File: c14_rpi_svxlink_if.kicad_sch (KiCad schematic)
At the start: 52 parts, among them J1 RPi_GPIO Tall, J2 Conn_01x04, J3 Conn_01x04, J4 Conn_01x04, J5 Conn_01x02, J6 Conn_01x04, J7 DB9F, Q1 BC847, Q2 BC847, Q3 BC847, Q4 BC857, T1 1:1, T2 1:1, U1 TLP222A o. AQY282EH, U2 HCPL-B17, U3 ADS1115_Module

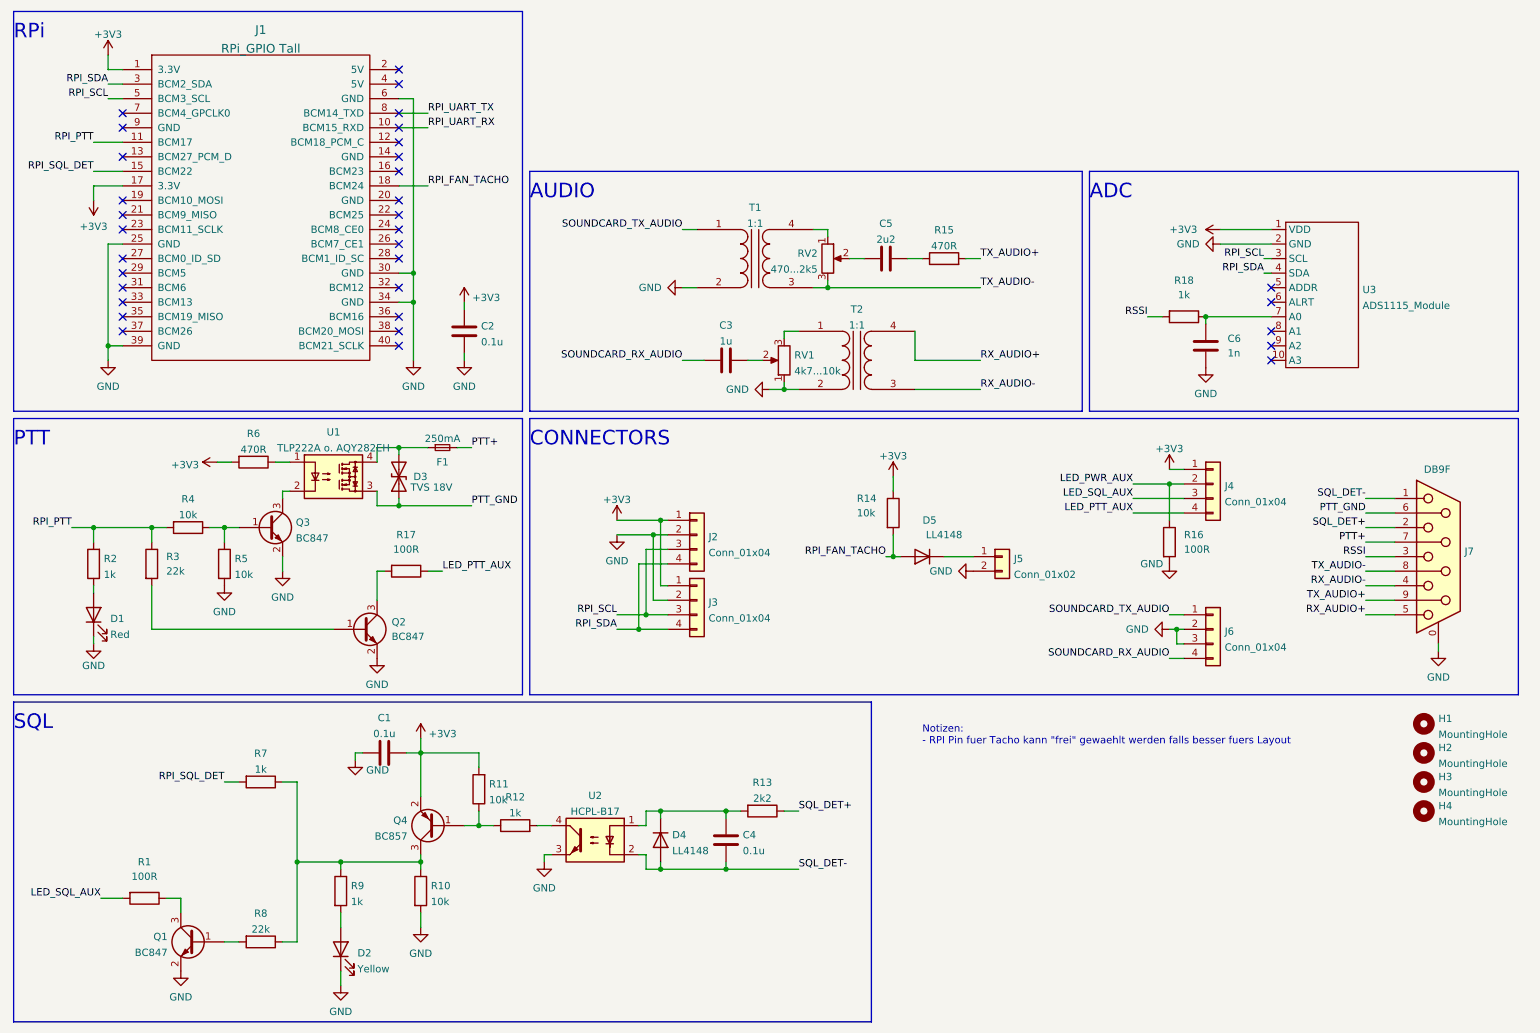
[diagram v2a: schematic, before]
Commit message: Add Open Collector for Fan Ctrl
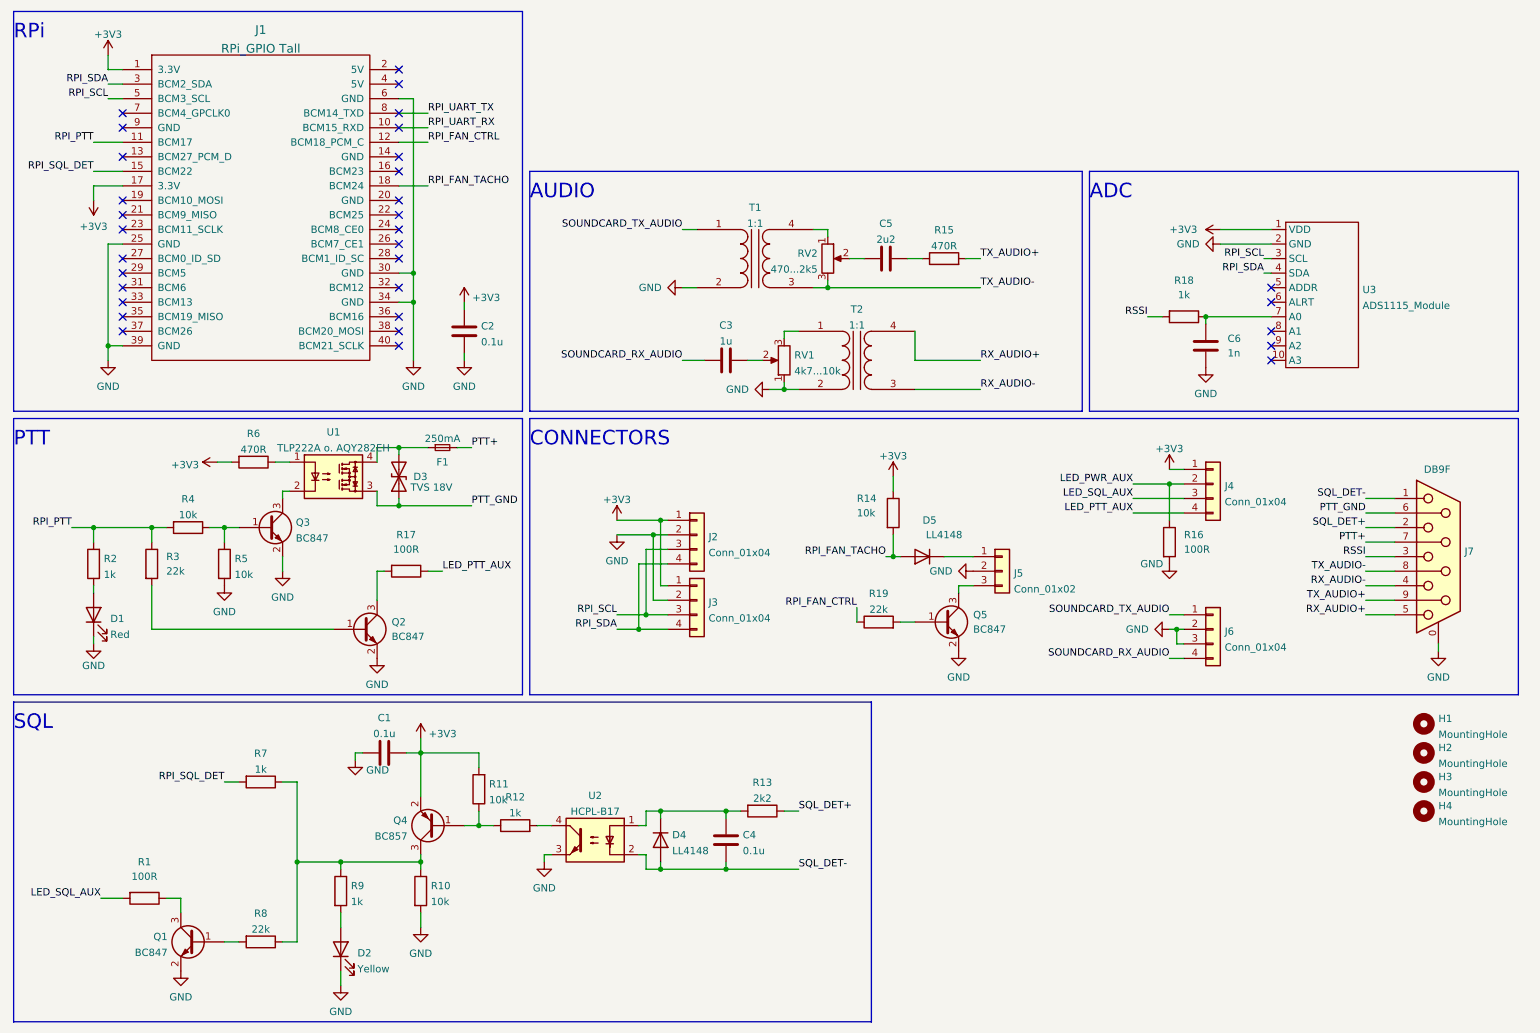
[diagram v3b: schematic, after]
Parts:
- added Q5: BC847, Package_TO_SOT_SMD:SOT-23, symbol Transistor_BJT:BC847
- added R19: 22k, Resistor_SMD:R_0805_2012Metric_Pad1.20x1.40mm_HandSolder, symbol Device:R
- J5: footprint Connector_JST:JST_XH_B2B-XH-A_1x02_P2.50mm_Vertical -> Connector_JST:JST_XH_B3B-XH-A_1x03_P2.50mm_Vertical; symbol Connector_Generic:Conn_01x02 -> Connector_Generic:Conn_01x03
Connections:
- net GND: now also Q5.2 (E)
- net RPI_FAN_CTRL: now reaches J1.12 (BCM18_PCM_C)
- net RPI_FAN_CTRL: now also R19.1
- new net: Q5.1 (B), R19.2
- new net: J5.3 (Pin_3), Q5.3 (C)
- no-connect marks 33 -> 32
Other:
- note removed: "Notizen: - RPI Pin fuer Tacho kann "frei" gewaehlt werden falls besser fuers Layout"
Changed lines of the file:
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@@
   (no_connect (at 86.36 77.47))
   (no_connect (at 86.36 54.61))
-  (no_connect (at 86.36 41.91))
-  (no_connect (at 86.36 46.99))
   (no_connect (at 86.36 52.07))
   (no_connect (at 238.76 67.31))
   (no_connect (at 86.36 31.75))
   (no_connect (at 86.36 29.21))
+  (no_connect (at 86.36 46.99))
   (no_connect (at 238.76 80.01))
   (no_connect (at 238.76 74.93))
@@
     (stroke (width 0) (type default) (color 0 0 0 0))
   )
+  (wire (pts (xy 184.15 119.38) (xy 184.15 120.65))
+    (stroke (width 0) (type default) (color 0 0 0 0))
+  )
   (wire (pts (xy 76.2 176.53) (xy 76.2 179.07))
     (stroke (width 0) (type default) (color 0 0 0 0))
@@
     (stroke (width 0) (type default) (color 0 0 0 0))
   )
+  (wire (pts (xy 86.36 41.91) (xy 91.44 41.91))
+    (stroke (width 0) (type default) (color 0 0 0 0))
+  )
   (wire (pts (xy 172.72 114.3) (xy 173.99 114.3))
     (stroke (width 0) (type default) (color 0 0 0 0))
@@
     (stroke (width 0) (type default) (color 0 0 0 0))
   )
+  (wire (pts (xy 173.99 125.73) (xy 176.53 125.73))
+    (stroke (width 0) (type default) (color 0 0 0 0))
+  )
   (wire (pts (xy 267.97 129.54) (xy 267.97 130.81))
     (stroke (width 0) (type default) (color 0 0 0 0))
   )
+  (wire (pts (xy 166.37 123.19) (xy 166.37 125.73))
+    (stroke (width 0) (type default) (color 0 0 0 0))
+  )
   (wire (pts (xy 181.61 114.3) (xy 186.69 114.3))
     (stroke (width 0) (type default) (color 0 0 0 0))
@@
   )
   (wire (pts (xy 43.18 127) (xy 74.93 127))
+    (stroke (width 0) (type default) (color 0 0 0 0))
+  )
+  (wire (pts (xy 186.69 119.38) (xy 184.15 119.38))
     (stroke (width 0) (type default) (color 0 0 0 0))
   )
@@
     (effects (font (size 2.54 2.54)) (justify left bottom))
   )
-  (text "Notizen:\n- RPI Pin fuer Tacho kann \"frei\" gewaehlt werden falls besser fuers Layout"
-    (at 177.8 147.32 0)
-    (effects (font (size 1.27 1.27)) (justify left bottom))
-  )
   (text "PTT" (at 19.05 95.25 0)
     (effects (font (size 2.54 2.54)) (justify left bottom))
@@
     (effects (font (size 1.27 1.27)) (justify left bottom))
   )
+  (label "RPI_FAN_CTRL" (at 91.44 41.91 0)
+    (effects (font (size 1.27 1.27)) (justify left bottom))
+  )
   (label "LED_SQL_AUX" (at 34.29 173.99 180)
     (effects (font (size 1.27 1.27)) (justify right bottom))
@@
   (label "SQL_DET-" (at 156.21 168.91 0)
     (effects (font (size 1.27 1.27)) (justify left bottom))
+  )
+  (label "RPI_FAN_CTRL" (at 166.37 123.19 180)
+    (effects (font (size 1.27 1.27)) (justify right bottom))
   )
   (label "PTT+" (at 255.27 111.76 180)
@@
     )
   )
+  (symbol (lib_id "Device:R") (at 170.18 125.73 90) (unit 1)
+    (in_bom yes) (on_board yes) (fields_autoplaced)
+    (property "Reference" "R19" (id 0) (at 170.18 120.7475 90))
+    (property "Value" "22k" (id 1) (at 170.18 123.5226 90))
+    (property "Footprint" "Resistor_SMD:R_0805_2012Metric_Pad1.20x1.40mm_HandSolder" (id 2) (at 170.18 127.508 90)
+      (effects (font (size 1.27 1.27)) hide)
+    )
+    (property "Datasheet" "~" (id 3) (at 170.18 125.73 0)
+      (effects (font (size 1.27 1.27)) hide)
+    )
+    (property "PartNr_Mouser" "603-RC0805FR-0722KL" (id 4) (at 170.18 125.73 0)
+      (effects (font (size 1.27 1.27)) hide)
+    )
+    (pin "1")
+    (pin "2")
+  )
   (symbol (lib_id "power:+3V3") (at 97.79 69.85 0) (unit 1)
     (in_bom yes) (on_board yes) (fields_autoplaced)
@@
     (pin "1")
   )
-  (symbol (lib_id "Connector_Generic:Conn_01x02") (at 191.77 114.3 0) (unit 1)
-    (in_bom yes) (on_board yes) (fields_autoplaced)
-    (property "Reference" "J5" (id 0) (at 193.802 114.6615 0)
-      (effects (font (size 1.27 1.27)) (justify left))
-    )
-    (property "Value" "Conn_01x02" (id 1) (at 193.802 117.4366 0)
-      (effects (font (size 1.27 1.27)) (justify left))
-    )
-    (property "Footprint" "Connector_JST:JST_XH_B2B-XH-A_1x02_P2.50mm_Vertical" (id 2) (at 191.77 114.3 0)
-      (effects (font (size 1.27 1.27)) hide)
-    )
-    (property "Datasheet" "~" (id 3) (at 191.77 114.3 0)
-      (effects (font (size 1.27 1.27)) hide)
-    )
-    (pin "1")
-    (pin "2")
+  (symbol (lib_id "Connector_Generic:Conn_01x03") (at 191.77 116.84 0) (unit 1)
+    (in_bom yes) (on_board yes) (fields_autoplaced)
+    (property "Reference" "J5" (id 0) (at 193.802 117.2015 0)
+      (effects (font (size 1.27 1.27)) (justify left))
+    )
+    (property "Value" "Conn_01x02" (id 1) (at 193.802 119.9766 0)
+      (effects (font (size 1.27 1.27)) (justify left))
+    )
+    (property "Footprint" "Connector_JST:JST_XH_B3B-XH-A_1x03_P2.50mm_Vertical" (id 2) (at 191.77 116.84 0)
+      (effects (font (size 1.27 1.27)) hide)
+    )
+    (property "Datasheet" "~" (id 3) (at 191.77 116.84 0)
+      (effects (font (size 1.27 1.27)) hide)
+    )
+    (pin "1")
+    (pin "2")
+    (pin "3")
   )
   (symbol (lib_id "Device:C") (at 143.51 80.01 270) (unit 1)
@@
     (pin "1")
   )
+  (symbol (lib_id "Transistor_BJT:BC847") (at 181.61 125.73 0) (unit 1)
+    (in_bom yes) (on_board yes) (fields_autoplaced)
+    (property "Reference" "Q5" (id 0) (at 186.69 124.4599 0)
+      (effects (font (size 1.27 1.27)) (justify left))
+    )
+    (property "Value" "BC847" (id 1) (at 186.69 126.9999 0)
+      (effects (font (size 1.27 1.27)) (justify left))
+    )
+    (property "Footprint" "Package_TO_SOT_SMD:SOT-23" (id 2) (at 186.69 127.635 0)
+      (effects (font (size 1.27 1.27) italic) (justify left) hide)
+    )
+    (property "Datasheet" "http://www.infineon.com/dgdl/Infineon-BC847SERIES_BC848SERIES_BC849SERIES_BC850SERIES-DS-v01_01-en.pdf?fileId=db3a304314dca389011541d4630a1657" (id 3) (at 181.61 125.73 0)
+      (effects (font (size 1.27 1.27)) (justify left) hide)
+    )
+    (property "PartNr_Mouser" "771-BC847235" (id 4) (at 181.61 125.73 0)
+      (effects (font (size 1.27 1.27)) hide)
+    )
+    (pin "1")
+    (pin "2")
+    (pin "3")
+  )
   (symbol (lib_id "Device:R") (at 60.96 97.79 270) (unit 1)
     (in_bom yes) (on_board yes) (fields_autoplaced)
@@
     (pin "2")
   )
+  (symbol (lib_id "power:GND") (at 184.15 130.81 0) (unit 1)
+    (in_bom yes) (on_board yes) (fields_autoplaced)
+    (property "Reference" "#PWR031" (id 0) (at 184.15 137.16 0)
+      (effects (font (size 1.27 1.27)) hide)
+    )
+    (property "Value" "GND" (id 1) (at 184.15 135.3725 0))
+    (property "Footprint" "" (id 2) (at 184.15 130.81 0)
+      (effects (font (size 1.27 1.27)) hide)
+    )
+    (property "Datasheet" "" (id 3) (at 184.15 130.81 0)
+      (effects (font (size 1.27 1.27)) hide)
+    )
+    (pin "1")
+  )
   (symbol (lib_id "power:GND") (at 78.74 149.86 0) (unit 1)
     (in_bom yes) (on_board yes) (fields_autoplaced)
@@
       (reference "#PWR030") (unit 1) (value "+3V3") (footprint "")
     )
+    (path "/d8fbedd9-bbf3-4187-842a-3510bcba1e5f"
+      (reference "#PWR031") (unit 1) (value "GND") (footprint "")
+    )
     (path "/d7715fde-6f0b-46cf-9dde-1798ae531e5a"
       (reference "C1") (unit 1) (value "0.1u") (footprint "Capacitor_SMD:C_0805_2012Metric_Pad1.18x1.45mm_HandSolder")
@@
     )
     (path "/58956415-360b-40f7-803b-b6f3cb064aa6"
-      (reference "J5") (unit 1) (value "Conn_01x02") (footprint "Connector_JST:JST_XH_B2B-XH-A_1x02_P2.50mm_Vertical")
+      (reference "J5") (unit 1) (value "Conn_01x02") (footprint "Connector_JST:JST_XH_B3B-XH-A_1x03_P2.50mm_Vertical")
     )
     (path "/529e174a-9525-49fa-9570-9a824abc0712"
@@
       (reference "Q4") (unit 1) (value "BC857") (footprint "Package_TO_SOT_SMD:SOT-23")
     )
+    (path "/98c41d91-3f72-4f82-8376-ce2f310a6d96"
+      (reference "Q5") (unit 1) (value "BC847") (footprint "Package_TO_SOT_SMD:SOT-23")
+    )
     (path "/9fee11bc-5830-4e56-b0e4-2a78e387f58b"
       (reference "R1") (unit 1) (value "100R") (footprint "Resistor_SMD:R_0805_2012Metric_Pad1.20x1.40mm_HandSolder")
@@
       (reference "R18") (unit 1) (value "1k") (footprint "Resistor_SMD:R_0805_2012Metric_Pad1.20x1.40mm_HandSolder")
     )
+    (path "/3fdc1205-170d-4bad-a583-c2274b810ac0"
+      (reference "R19") (unit 1) (value "22k") (footprint "Resistor_SMD:R_0805_2012Metric_Pad1.20x1.40mm_HandSolder")
+    )
     (path "/54545e51-e802-4511-9bf4-469b9f2f2d3a"

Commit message: Neue Teile platziert, pre-1.1 bereit fuer Review
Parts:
- removed Q5: BC847, Package_TO_SOT_SMD:SOT-23, symbol Transistor_BJT:BC847
- added C7, C8: 1n, Capacitor_SMD:C_0805_2012Metric_Pad1.18x1.45mm_HandSolder, symbol Device:C
- added D6, D7: LL4148, Diode_SMD:D_MiniMELF, symbol Diode:LL4148
- added FID1, FID2, FID3: Fiducial, Fiducial:Fiducial_1mm_Mask3mm, symbol Mechanical:Fiducial
- added J8: Conn_01x01_Male, Connector_PinHeader_2.54mm:PinHeader_1x01_P2.54mm_Vertical, symbol Connector:Conn_01x01_Male
- added JP1, JP2: SolderJumper_2_Open, Jumper:SolderJumper-2_P1.3mm_Open_TrianglePad1.0x1.5mm, symbol Jumper:SolderJumper_2_Open
- added LOGO1: Logo_Open_Hardware_Small, Symbol:OSHW-Logo2_9.8x8mm_SilkScreen, symbol Graphic:Logo_Open_Hardware_Small
- added Q5: IRLML0030, Package_TO_SOT_SMD:SOT-23, symbol Transistor_FET:IRLML0030
- added R20: 10k, Resistor_SMD:R_0805_2012Metric_Pad1.20x1.40mm_HandSolder, symbol Device:R
- added TP1: Conn_01x09_Male, Connector_PinHeader_1.27mm:PinHeader_1x09_P1.27mm_Vertical, symbol Connector:Conn_01x09_Male
- added TP2: Conn_01x03_Male, Connector_PinHeader_1.27mm:PinHeader_1x03_P1.27mm_Vertical, symbol Connector:Conn_01x03_Male
- R19: value 22k -> 1k
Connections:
- net GND: now also J8.1 (Pin_1), JP1.1 (A), Q5.2 (S), R20.2, TP2.2 (Pin_2)
- net PTT+: now also TP1.4 (Pin_4)
- net PTT_GND: now also TP1.2 (Pin_2)
- net RPI_FAN_CTRL: now also R20.1
- net RSSI: now also TP1.5 (Pin_5)
- net RX_AUDIO+: now also C8.2, JP2.2 (B), TP1.9 (Pin_9)
- net RX_AUDIO-: now also C8.1, D6.1 (K), D7.2 (A), TP1.7 (Pin_7)
- net SOUNDCARD_RX_AUDIO: now also TP2.3 (Pin_3)
- net SOUNDCARD_TX_AUDIO: now also TP2.1 (Pin_1)
- net SQL_DET+: now also TP1.3 (Pin_3)
- net SQL_DET-: now also TP1.1 (Pin_1)
- net TX_AUDIO+: now also C7.2, TP1.8 (Pin_8)
- net TX_AUDIO-: now also C7.1, TP1.6 (Pin_6)
- net at R19.2: now also Q5.1 (G)
- net at J5.1 (Pin_1): now also JP1.2 (B), Q5.3 (D); no longer D5.1 (K)
- net at J5.3 (Pin_3): now also D5.1 (K)
- new net: D6.2 (A), D7.1 (K), JP2.1 (A)
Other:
- moved on the sheet: C3, D5, J5, J6, J7, R14, R15, R19, RV1, T2

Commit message: ready for production
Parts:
- added C9: 1n, Capacitor_SMD:C_0805_2012Metric_Pad1.18x1.45mm_HandSolder, symbol Device:C
- added R21: 100R, Resistor_SMD:R_0805_2012Metric_Pad1.20x1.40mm_HandSolder, symbol Device:R
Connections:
- net GND: now also C9.1
- net at Q5.1 (G), R19.2: now also C9.2
- net at D6.2 (A), D7.1 (K): now also R21.2; no longer JP2.1 (A)
- new net: JP2.1 (A), R21.1
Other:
- moved on the sheet: J2, J3, R19, R20

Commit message: last changes for 1.1
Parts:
- Q5: PartNr_Mouser (none) -> 942-IRLML0030TRPBF
- R19: PartNr_Mouser 603-RC0805FR-0722KL -> 652-CR0805FX-1001ELF
- R20: PartNr_Mouser (none) -> 603-RC0805JR-0710KL
- R21: PartNr_Mouser 652-CR0805FX-4700ELF -> 603-RC0805JR-07100RL
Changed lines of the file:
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@@
+      (effects (font (size 1.27 1.27)) hide)
+    )
+    (property "PartNr_Mouser" "603-RC0805JR-0710KL" (id 4) (at 156.21 129.54 0)
       (effects (font (size 1.27 1.27)) hide)
     )
@@
       (effects (font (size 1.27 1.27)) hide)
     )
-    (property "PartNr_Mouser" "603-RC0805FR-0722KL" (id 4) (at 161.29 124.46 0)
+    (property "PartNr_Mouser" "652-CR0805FX-1001ELF" (id 4) (at 161.29 124.46 0)
       (effects (font (size 1.27 1.27)) hide)
     )
@@
       (effects (font (size 1.27 1.27)) (justify left) hide)
     )
+    (property "PartNr_Mouser" "942-IRLML0030TRPBF" (id 4) (at 181.61 124.46 0)
+      (effects (font (size 1.27 1.27)) hide)
+    )
     (pin "1")
     (pin "2")
@@
       (effects (font (size 1.27 1.27)) hide)
     )
-    (property "PartNr_Mouser" "652-CR0805FX-4700ELF" (id 4) (at 170.18 77.47 0)
-      (effects (font (size 1.27 1.27)) hide)
-    )
+    (property "PartNr_Mouser" "603-RC0805JR-07100RL" (id 4) (at 170.18 77.47 0)
+      (effects (font (size 1.27 1.27)) hide)
+    )
